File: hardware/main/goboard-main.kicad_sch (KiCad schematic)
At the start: 12 parts, among them J1 USB_C_Receptacle_USB2.0

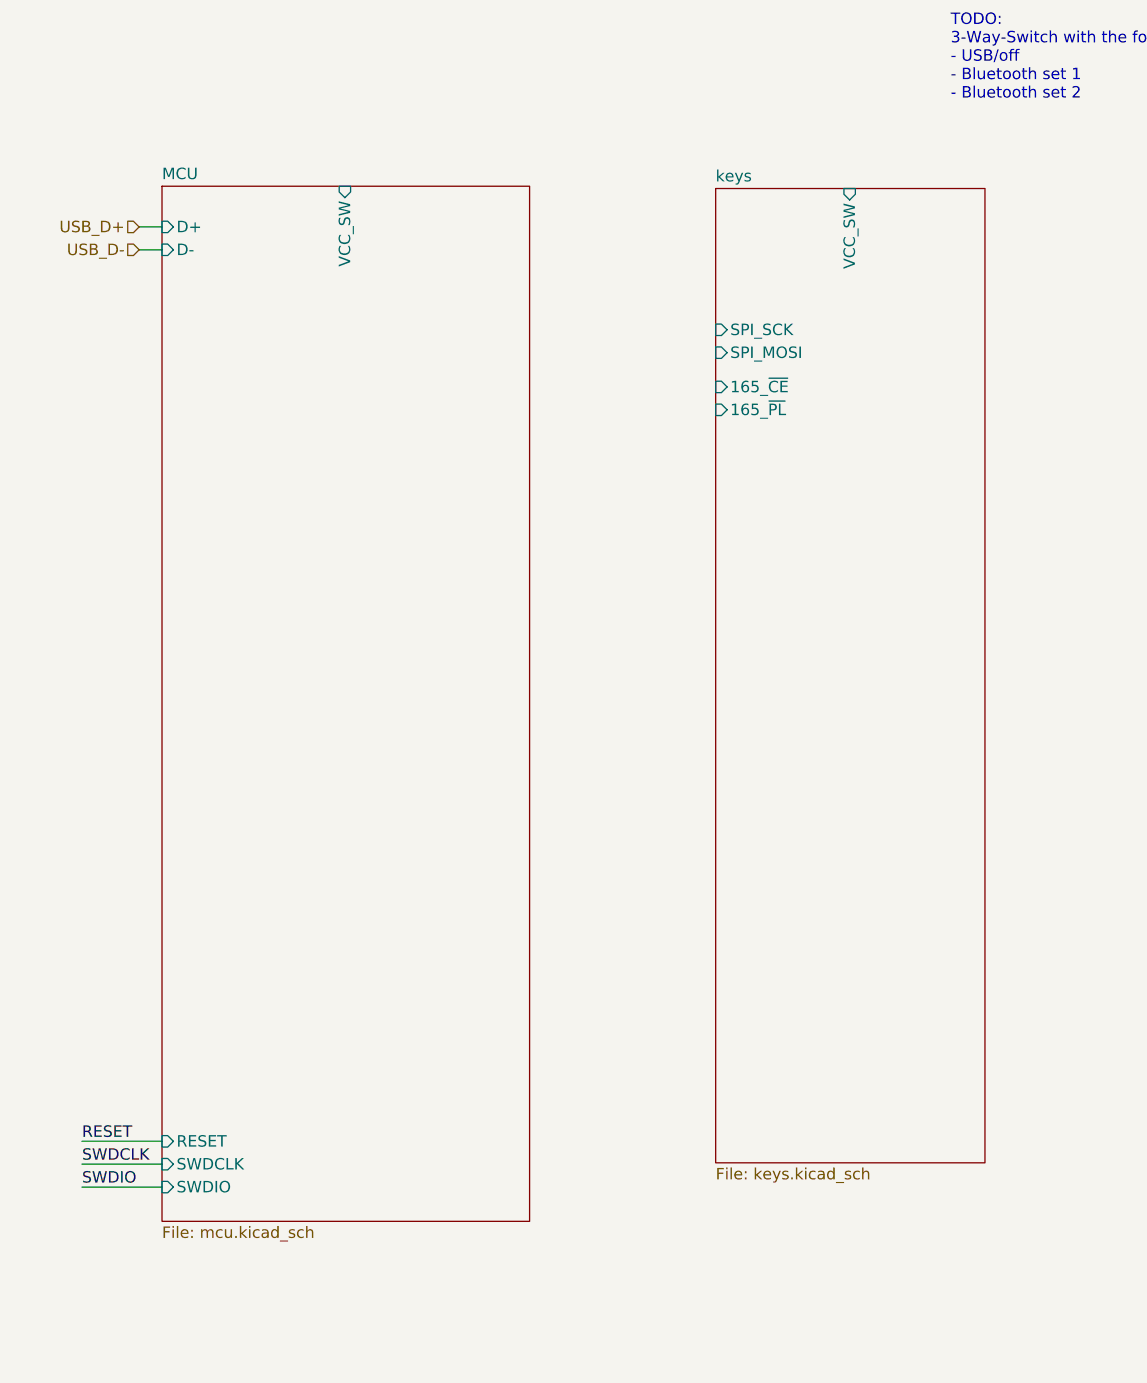
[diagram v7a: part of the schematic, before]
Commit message: Add connections to the NRF module
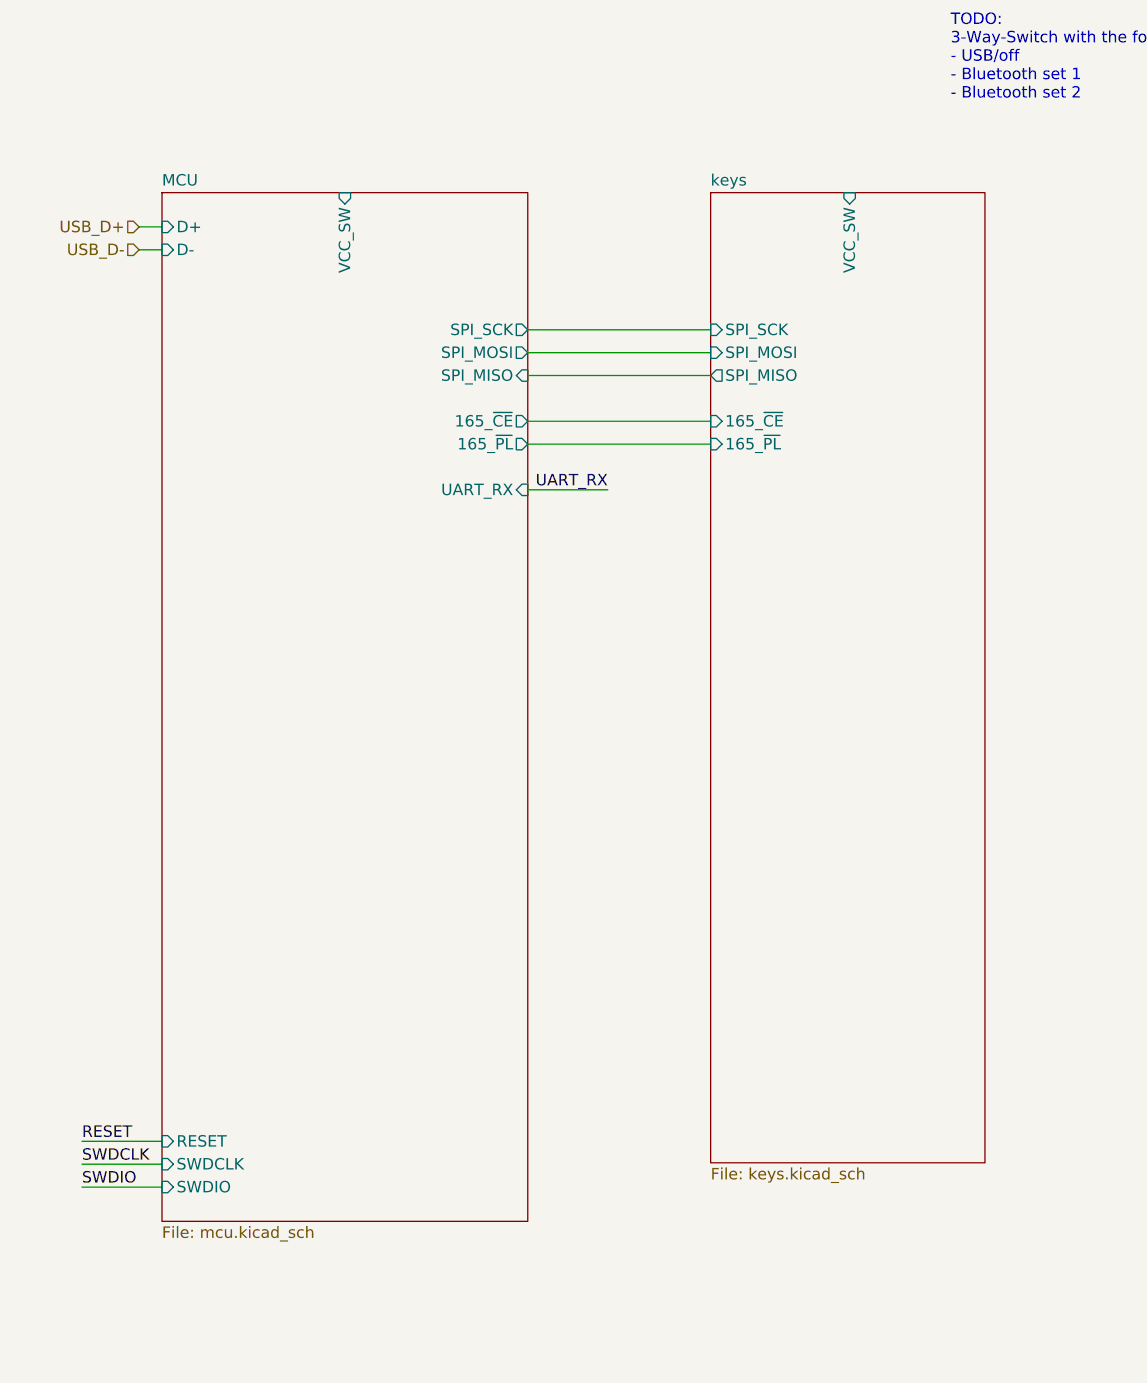
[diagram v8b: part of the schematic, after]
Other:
- sheet MCU ports: added 165_~CE, 165_~PL, SPI_MISO, SPI_MOSI, SPI_SCK, UART_RX; removed none
- sheet keys ports: added SPI_MISO; removed none
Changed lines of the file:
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@@
+    (stroke (width 0) (type solid) (color 0 0 0 0))
+  )
+  (wire (pts (xy 161.29 54.61) (xy 181.61 54.61))
+    (stroke (width 0) (type solid) (color 0 0 0 0))
+  )
+  (wire (pts (xy 161.29 57.15) (xy 181.61 57.15))
+    (stroke (width 0) (type solid) (color 0 0 0 0))
+  )
+  (wire (pts (xy 161.29 59.69) (xy 181.61 59.69))
+    (stroke (width 0) (type solid) (color 0 0 0 0))
+  )
+  (wire (pts (xy 161.29 64.77) (xy 181.61 64.77))
+    (stroke (width 0) (type solid) (color 0 0 0 0))
+  )
+  (wire (pts (xy 161.29 67.31) (xy 181.61 67.31))
+    (stroke (width 0) (type solid) (color 0 0 0 0))
+  )
+  (wire (pts (xy 161.29 72.39) (xy 170.18 72.39))
     (stroke (width 0) (type solid) (color 0 0 0 0))
   )
@@
   (label "SWDIO" (at 111.76 149.86 0)
     (effects (font (size 1.27 1.27)) (justify left bottom))
+  )
+  (label "UART_RX" (at 170.18 72.39 180)
+    (effects (font (size 1.27 1.27)) (justify right bottom))
   )
   (label "VCC_SW_NUMPAD" (at 242.57 132.08 0)
@@
     )
   )
-  (sheet (at 120.65 38.6588) (size 40.8432 115.0112)
+  (sheet (at 120.65 39.37) (size 40.64 114.3)
     (stroke (width 0.001) (type solid) (color 132 0 132 1))
     (fill (color 255 255 255 0.0000))
-    (property "Schaltplanname" "MCU" (id 0) (at 120.65 38.0229 0)
+    (property "Schaltplanname" "MCU" (id 0) (at 120.65 38.7341 0)
       (effects (font (size 1.27 1.27)) (justify left bottom))
     )
@@
       (effects (font (size 1.27 1.27)) (justify left top))
     )
-    (pin "VCC_SW" input (at 140.97 38.6588 90)
+    (pin "VCC_SW" input (at 140.97 39.37 90)
       (effects (font (size 1.27 1.27)) (justify right))
     )
@@
     (pin "RESET" input (at 120.65 144.78 180)
       (effects (font (size 1.27 1.27)) (justify left))
+    )
+    (pin "UART_RX" input (at 161.29 72.39 0)
+      (effects (font (size 1.27 1.27)) (justify right))
+    )
+    (pin "SPI_MISO" input (at 161.29 59.69 0)
+      (effects (font (size 1.27 1.27)) (justify right))
+    )
+    (pin "SPI_SCK" output (at 161.29 54.61 0)
+      (effects (font (size 1.27 1.27)) (justify right))
+    )
+    (pin "SPI_MOSI" output (at 161.29 57.15 0)
+      (effects (font (size 1.27 1.27)) (justify right))
+    )
+    (pin "165_~CE" output (at 161.29 64.77 0)
+      (effects (font (size 1.27 1.27)) (justify right))
+    )
+    (pin "165_~PL" output (at 161.29 67.31 0)
+      (effects (font (size 1.27 1.27)) (justify right))
     )
   )
@@
     )
   )
-  (sheet (at 182.1688 38.9128) (size 29.9212 108.2548)
+  (sheet (at 181.61 39.37) (size 30.48 107.7976)
     (stroke (width 0.001) (type solid) (color 132 0 132 1))
     (fill (color 255 255 255 0.0000))
-    (property "Schaltplanname" "keys" (id 0) (at 182.1688 38.2769 0)
+    (property "Schaltplanname" "keys" (id 0) (at 181.61 38.7341 0)
       (effects (font (size 1.27 1.27)) (justify left bottom))
     )
-    (property "Dateiname Blatt" "keys.kicad_sch" (id 1) (at 182.1688 147.6765 0)
+    (property "Dateiname Blatt" "keys.kicad_sch" (id 1) (at 181.61 147.6765 0)
       (effects (font (size 1.27 1.27)) (justify left top))
     )
-    (pin "VCC_SW" input (at 197.0532 38.9128 90)
-      (effects (font (size 1.27 1.27)) (justify right))
-    )
-    (pin "SPI_SCK" input (at 182.1688 54.61 180)
-      (effects (font (size 1.27 1.27)) (justify left))
-    )
-    (pin "SPI_MOSI" input (at 182.1688 57.15 180)
-      (effects (font (size 1.27 1.27)) (justify left))
-    )
-    (pin "165_~CE" input (at 182.1688 60.96 180)
-      (effects (font (size 1.27 1.27)) (justify left))
-    )
-    (pin "165_~PL" input (at 182.1688 63.5 180)
+    (pin "VCC_SW" input (at 197.0532 39.37 90)
+      (effects (font (size 1.27 1.27)) (justify right))
+    )
+    (pin "SPI_SCK" input (at 181.61 54.61 180)
+      (effects (font (size 1.27 1.27)) (justify left))
+    )
+    (pin "SPI_MOSI" input (at 181.61 57.15 180)
+      (effects (font (size 1.27 1.27)) (justify left))
+    )
+    (pin "165_~CE" input (at 181.61 64.77 180)
+      (effects (font (size 1.27 1.27)) (justify left))
+    )
+    (pin "165_~PL" input (at 181.61 67.31 180)
+      (effects (font (size 1.27 1.27)) (justify left))
+    )
+    (pin "SPI_MISO" output (at 181.61 59.69 180)
       (effects (font (size 1.27 1.27)) (justify left))
     )
@@
       (reference "#PWR0109") (unit 1) (value "GND") (footprint "")
     )
+    (path "/d1d7b976-c206-4a6a-bf43-9e0a3d3fc0a5/456c5560-5e5c-458e-a7f7-e577da6fbd17"
+      (reference "#PWR?") (unit 1) (value "GND") (footprint "")
+    )
     (path "/d1d7b976-c206-4a6a-bf43-9e0a3d3fc0a5/5d0f01e6-3cac-4a3c-9bd2-0ba422ba5ad9"
       (reference "#PWR?") (unit 1) (value "GND") (footprint "")
     )
+    (path "/d1d7b976-c206-4a6a-bf43-9e0a3d3fc0a5/6aefb866-3f31-45fc-835d-9e0d0ee3041d"
+      (reference "#PWR?") (unit 1) (value "GND") (footprint "")
+    )
+    (path "/d1d7b976-c206-4a6a-bf43-9e0a3d3fc0a5/ac41e8bc-33f1-480a-9578-3f27442f4e39"
+      (reference "#PWR?") (unit 1) (value "GND") (footprint "")
+    )
